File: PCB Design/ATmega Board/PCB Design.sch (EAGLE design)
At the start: 33 parts

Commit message: Before renumbering parts
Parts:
- removed JP3: (no value), pinhead:PINHD-1X7
- removed PORT_B, PORT_C: (no value), pinhead:PINHD-1X6
- removed PORT_D: (no value), pinhead:PINHD-1X8
- added JP4, JP5: (no value), pinhead:PINHD-2X6
- added JP6: (no value), pinhead:PINHD-2X8
- added JP7: (no value), pinhead:PINHD-2X3
- added R5: 330, resistor:R-EU_M0805
- added RX, TX: BLUE, SparkFun-LED:LED-BLUE0603
- JP1: device pinhead:PINHD-1X3 -> pinhead:PINHD-2X7
- R2: value 220 -> 330
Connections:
- new net N$3: R5.2, RX.C
- net +5V: now also JP1.2, JP7.1, JP7.2, LCD.VDD; no longer JP3.1, R2.1
- net 3.3V: now also JP1.5, JP1.6; no longer JP3.3
- net AREF: now also JP1.7, JP1.8, JP7.3, JP7.4; no longer JP1.2, JP3.4
- net GND: now also JP1.4, JP7.5, JP7.6, R2.1, R5.1; no longer JP3.2
- net N$7: now also TX.C; no longer LCD.VDD
- net PB0/D8: now also JP5.1, JP5.2; no longer PORT_B.1
- net PB1/D9: now also JP5.3, JP5.4; no longer PORT_B.2
- net PB2/D10: now also JP5.5, JP5.6; no longer PORT_B.3
- net PB3/MOSI/D11: now also JP5.7, JP5.8; no longer PORT_B.4
- net PB4/MISO/D12: now also JP5.10, JP5.9; no longer PORT_B.5
- net PB5/SCK/D13: now also JP5.11, JP5.12; no longer PORT_B.6
- net PC0/A0: now also JP4.1, JP4.2; no longer PORT_C.1
- net PC1/A1: now also JP4.3, JP4.4; no longer PORT_C.2
- net PC2/A2: now also JP4.5, JP4.6; no longer PORT_C.3
- net PC3/A3: now also JP4.7, JP4.8; no longer PORT_C.4
- net PC4/A4/SDA: now also JP1.13, JP1.14, JP4.10, JP4.9; no longer JP3.7, PORT_C.5
- net PC5/A5/SCL: now also JP1.11, JP1.12, JP4.11, JP4.12; no longer JP3.6, PORT_C.6
- net PC6/RESET: now also JP1.10, JP1.9; no longer JP3.5
- net PD0/RX: now also JP6.1, JP6.2, RX.A; no longer PORT_D.1
- net PD1/TX: now also JP6.3, JP6.4, TX.A; no longer PORT_D.2
- net PD2/LCD_D7: now also JP6.5, JP6.6; no longer PORT_D.3
- net PD3/LCD_D6: now also JP6.7, JP6.8; no longer PORT_D.4
- net PD4/LCD_D5: now also JP6.10, JP6.9; no longer PORT_D.5
- net PD5/LCD_D4: now also JP6.11, JP6.12; no longer PORT_D.6
- net PD6/LCD_E: now also JP6.13, JP6.14; no longer PORT_D.7
- net PD7/LCD_RS: now also JP6.15, JP6.16; no longer PORT_D.8

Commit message: Final
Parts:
- removed JP7: (no value), pinhead:PINHD-2X3
- added JP3: (no value), pinhead:PINHD-2X6
- C10: value 10uf -> .1uF; device resistor:CPOL-EUE2.5-6 -> rcl:C-EUC0805K
- C2: value 0.33µF -> .1uF
- C3: value 22pF -> .1uF
- C4: value 22pF -> 0.33µF
- C5, C6: value .1uF -> 22pF
- C8: value .1uF -> 10uf; device rcl:C-EUC0805K -> resistor:CPOL-EUE2.5-6
- JP1: device pinhead:PINHD-2X7 -> pinhead:PINHD-1X2
- JP2: device pinhead:PINHD-1X2 -> pinhead:PINHD-2X8
- JP5: device pinhead:PINHD-2X6 -> pinhead:PINHD-2X3
- JP6: device pinhead:PINHD-2X8 -> pinhead:PINHD-2X7
- R1: value 10k -> 330
- R3: value 330 -> 10k
- RX, TX: value BLUE -> Yellow
- renumbered 12V_JACK to 12V_DC, C13 to C7, CRYSTAL to Q1, LCD to LCD1, R15 to R7
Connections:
- net +12V: now also JP1.1; no longer JP2.1
- net +5V: now also C2.1, C3.1, JP5.1, JP5.2, JP6.1, JP6.2, R3.1; no longer C5.1, C8.1, JP1.1, JP1.2, JP7.1, JP7.2, R1.1
- net 3.3V: now also C8.+, JP6.5, JP6.6; no longer C10.+, JP1.5, JP1.6
- net AREF: now also C10.1, JP5.3, JP5.4, JP6.7, JP6.8; no longer C6.1, JP1.7, JP1.8, JP7.3, JP7.4
- net DTR: now also C4.2; no longer C2.2
- net GND: now also C10.2, C2.2, C3.2, C5.1, C6.1, C8.-, JP1.2, JP5.5, JP5.6, JP6.3, JP6.4, R1.1; no longer C10.-, C3.1, C4.1, C5.2, C6.2, C8.2, JP1.3, JP1.4, JP2.2, JP7.5, JP7.6, R3.1
- net N$1: now also R4.2; no longer R3.2
- net N$2: now also R5.2; no longer R4.2
- net N$3: now also R2.2; no longer R5.2
- net N$7: now also R1.2; no longer R2.2
- net PB0/D8: now also JP4.1, JP4.2; no longer JP5.1, JP5.2
- net PB1/D9: now also JP4.3, JP4.4; no longer JP5.3, JP5.4
- net PB2/D10: now also JP4.5, JP4.6; no longer JP5.5, JP5.6
- net PB3/MOSI/D11: now also JP4.7, JP4.8; no longer JP5.7, JP5.8
- net PB4/MISO/D12: now also JP4.10, JP4.9; no longer JP5.10, JP5.9
- net PB5/SCK/D13: now also JP4.11, JP4.12; no longer JP5.11, JP5.12
- net PB6/CRYSTAL1: now also C5.2; no longer C3.2
- net PB7/CRYSTAL2: now also C6.2; no longer C4.2
- net PC0/A0: now also JP3.1, JP3.2; no longer JP4.1, JP4.2
- net PC1/A1: now also JP3.3, JP3.4; no longer JP4.3, JP4.4
- net PC2/A2: now also JP3.5, JP3.6; no longer JP4.5, JP4.6
- net PC3/A3: now also JP3.7, JP3.8; no longer JP4.7, JP4.8
- net PC4/A4/SDA: now also JP3.10, JP3.9, JP6.13, JP6.14; no longer JP1.13, JP1.14, JP4.10, JP4.9
- net PC5/A5/SCL: now also JP3.11, JP3.12, JP6.11, JP6.12; no longer JP1.11, JP1.12, JP4.11, JP4.12
- net PC6/RESET: now also C4.1, JP6.10, JP6.9, R3.2; no longer C2.1, JP1.10, JP1.9, R1.2
- net PD0/RX: now also JP2.1, JP2.2; no longer JP6.1, JP6.2
- net PD1/TX: now also JP2.3, JP2.4; no longer JP6.3, JP6.4
- net PD2/LCD_D7: now also JP2.5, JP2.6; no longer JP6.5, JP6.6
- net PD3/LCD_D6: now also JP2.7, JP2.8; no longer JP6.7, JP6.8
- net PD4/LCD_D5: now also JP2.10, JP2.9; no longer JP6.10, JP6.9
- net PD5/LCD_D4: now also JP2.11, JP2.12; no longer JP6.11, JP6.12
- net PD6/LCD_E: now also JP2.13, JP2.14; no longer JP6.13, JP6.14
- net PD7/LCD_RS: now also JP2.15, JP2.16; no longer JP6.15, JP6.16

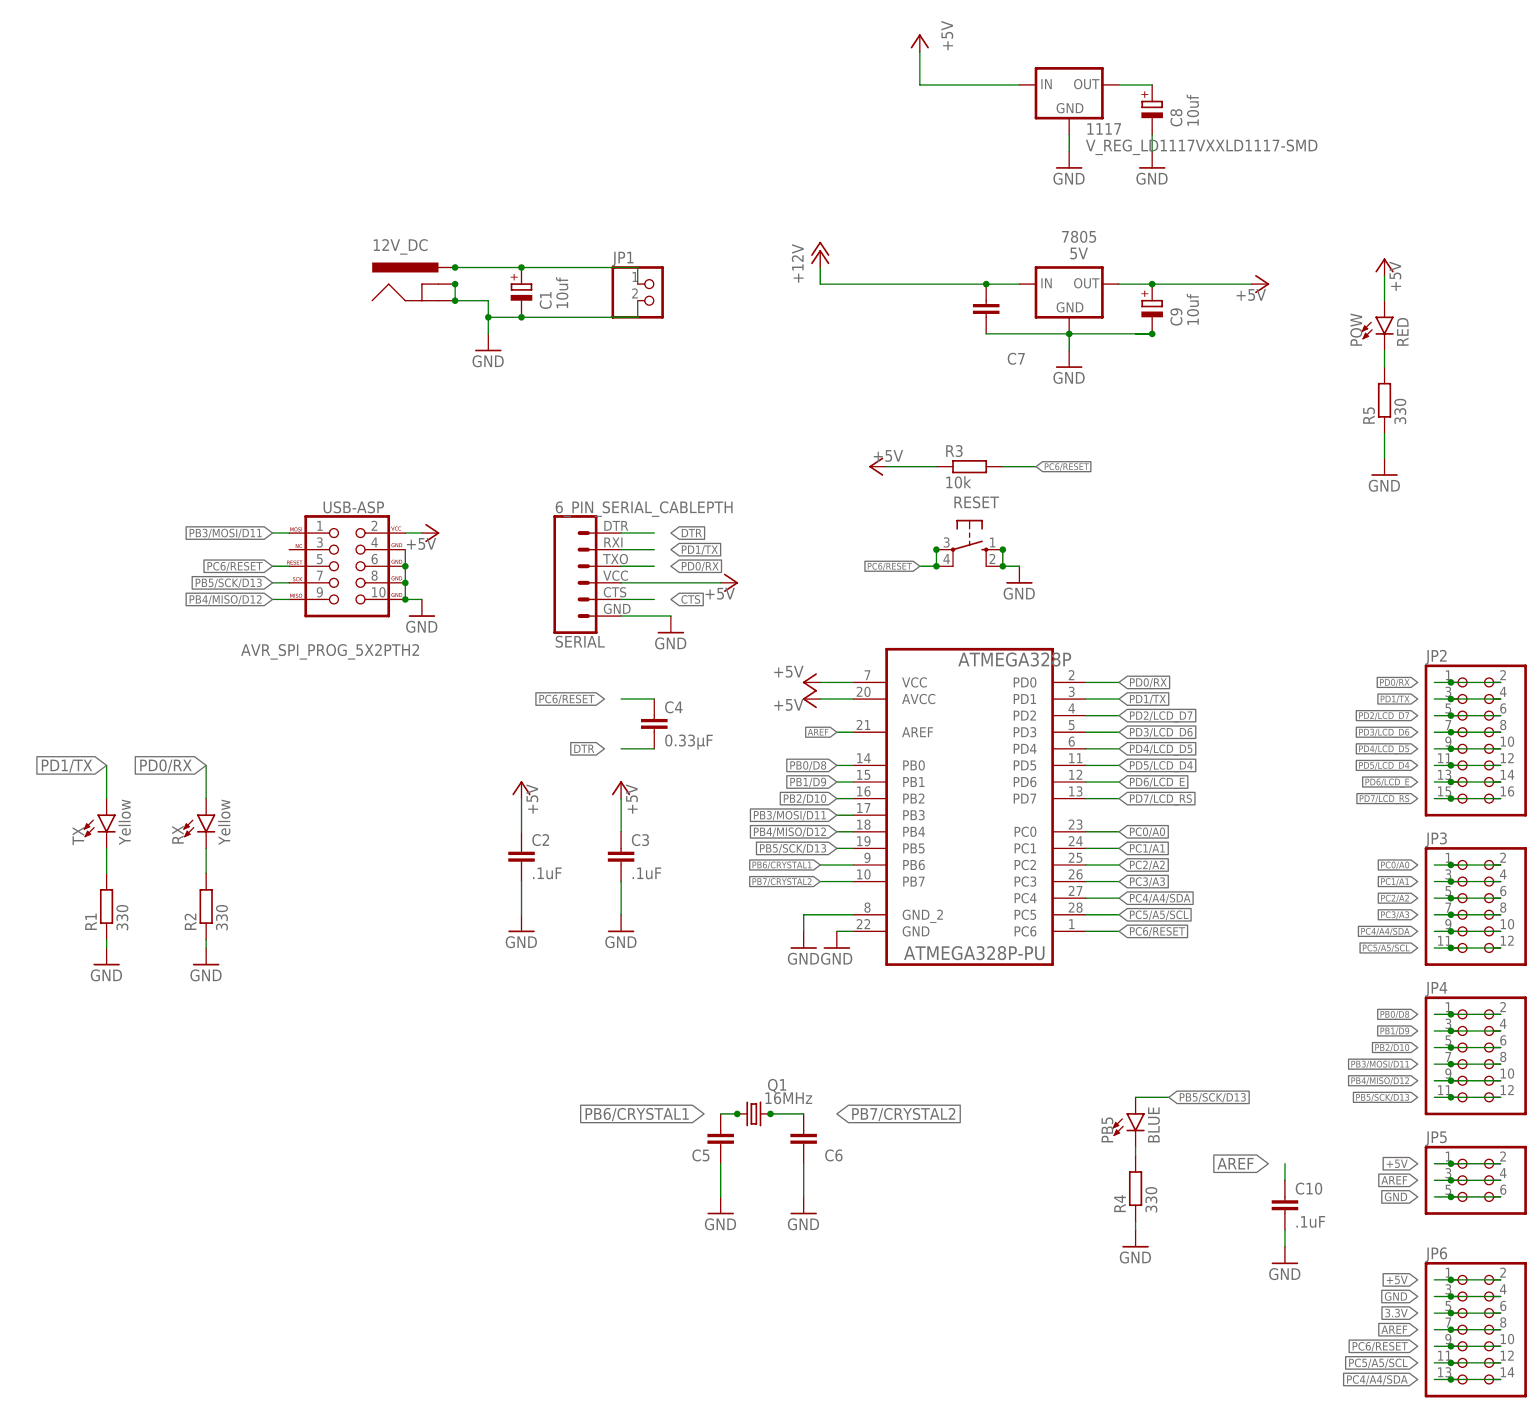
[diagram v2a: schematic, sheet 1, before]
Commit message: Corrected Silkscreen
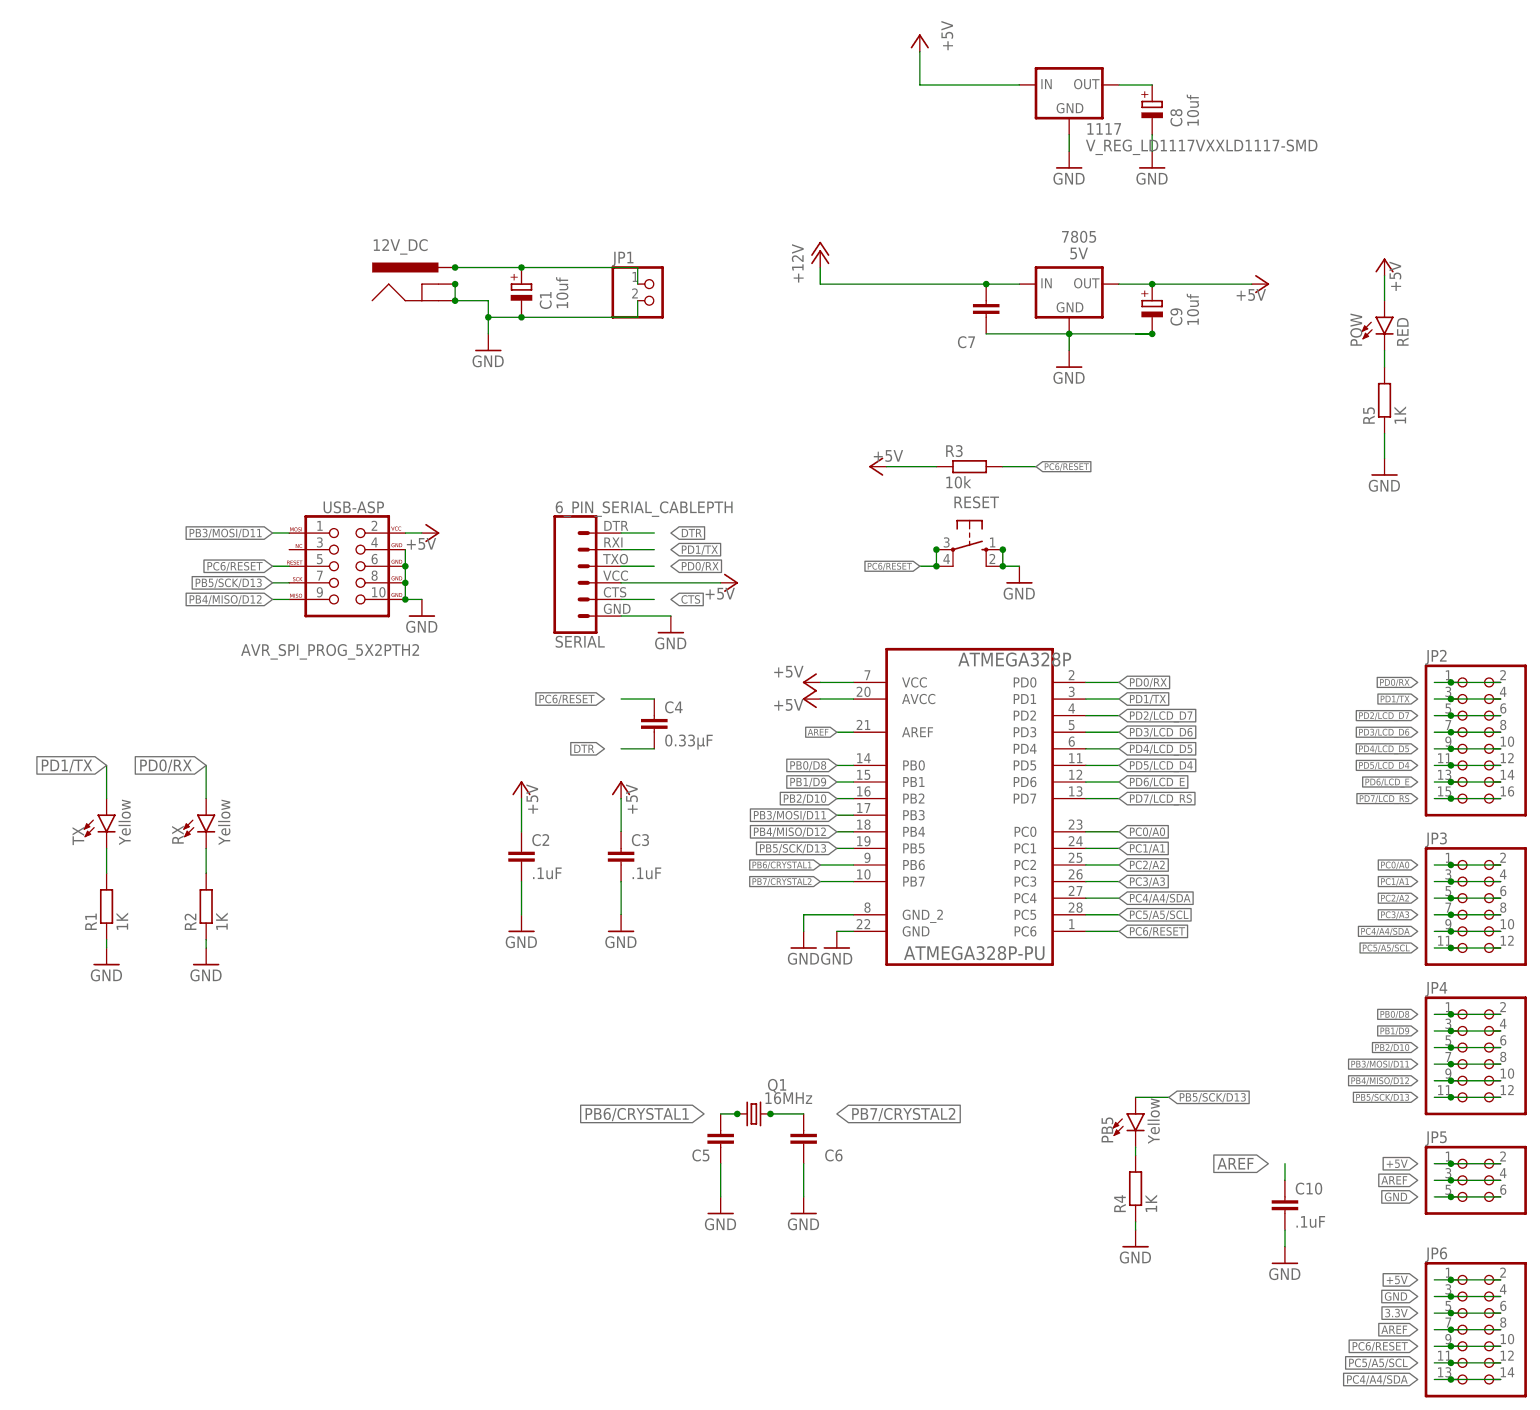
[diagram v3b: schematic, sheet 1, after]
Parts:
- 1117, 7805, C1, C10, C2, C3, C4, C5, C6, C7, C8, C9, CONT, JP1, JP2, JP3, JP4, JP5, JP6, LCD1, POW, R3, R7, RX, SERIAL, TX, USB-ASP: OC_FARNELL (none) -> unknown
- 12V_DC: MF (none) -> MULTICOMP; MPN (none) -> SPC21365; OC_FARNELL (none) -> 1310918
- ATMEGA328P: MF (none) -> MICROCHIP
- PB5: value BLUE -> Yellow; OC_FARNELL (none) -> unknown
- R1, R2, R4, R5: value 330 -> 1K; OC_FARNELL (none) -> unknown
- RESET: MF (none) -> OMRON ELECTRONIC COMPONENTS
